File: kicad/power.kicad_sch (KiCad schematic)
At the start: 52 parts, among them P1 VBAT, P2 GND, P3 10V, P4 GND, Q2 NX7002AK, U1 LMR38020FSDDAR, U2 LMR38020FSDDAR, U4 LP38692MP-3.3, U5 LP5907MFX-3.3

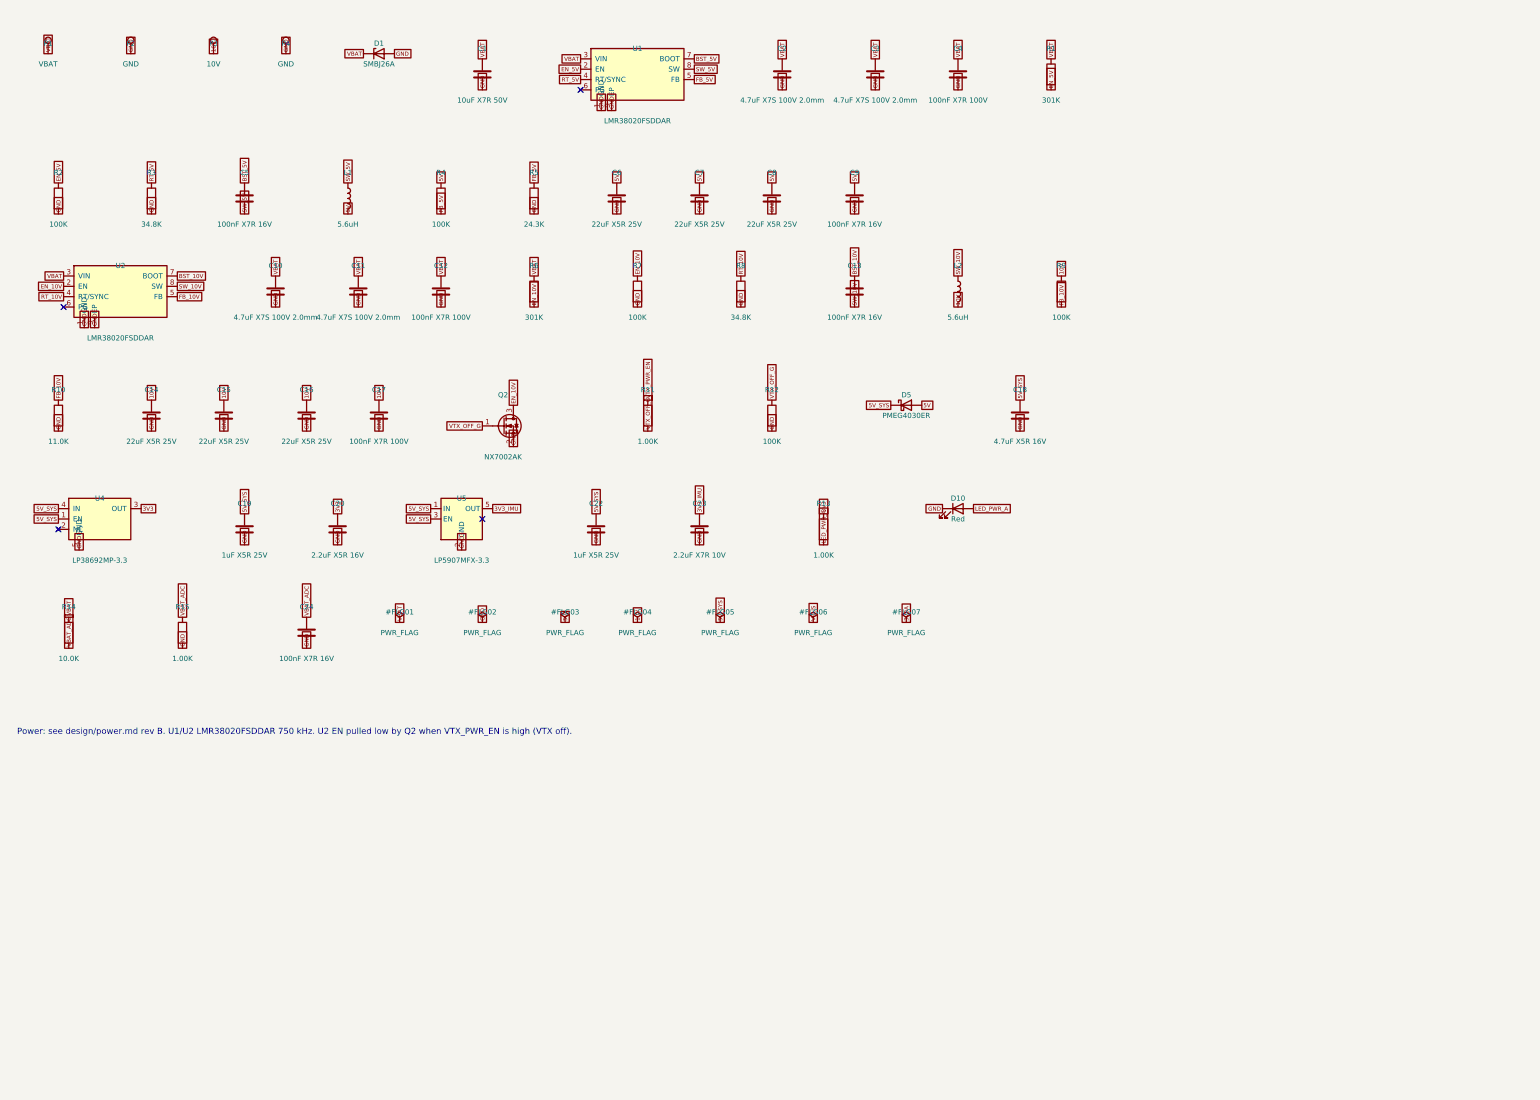
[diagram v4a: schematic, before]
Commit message: Readable schematic: functional blocks with titles, passives wired to their IC pins, GND power symbols, per-rail decoupling banks, labels only between blocks (ERC 0, netcheck OK, same nets)
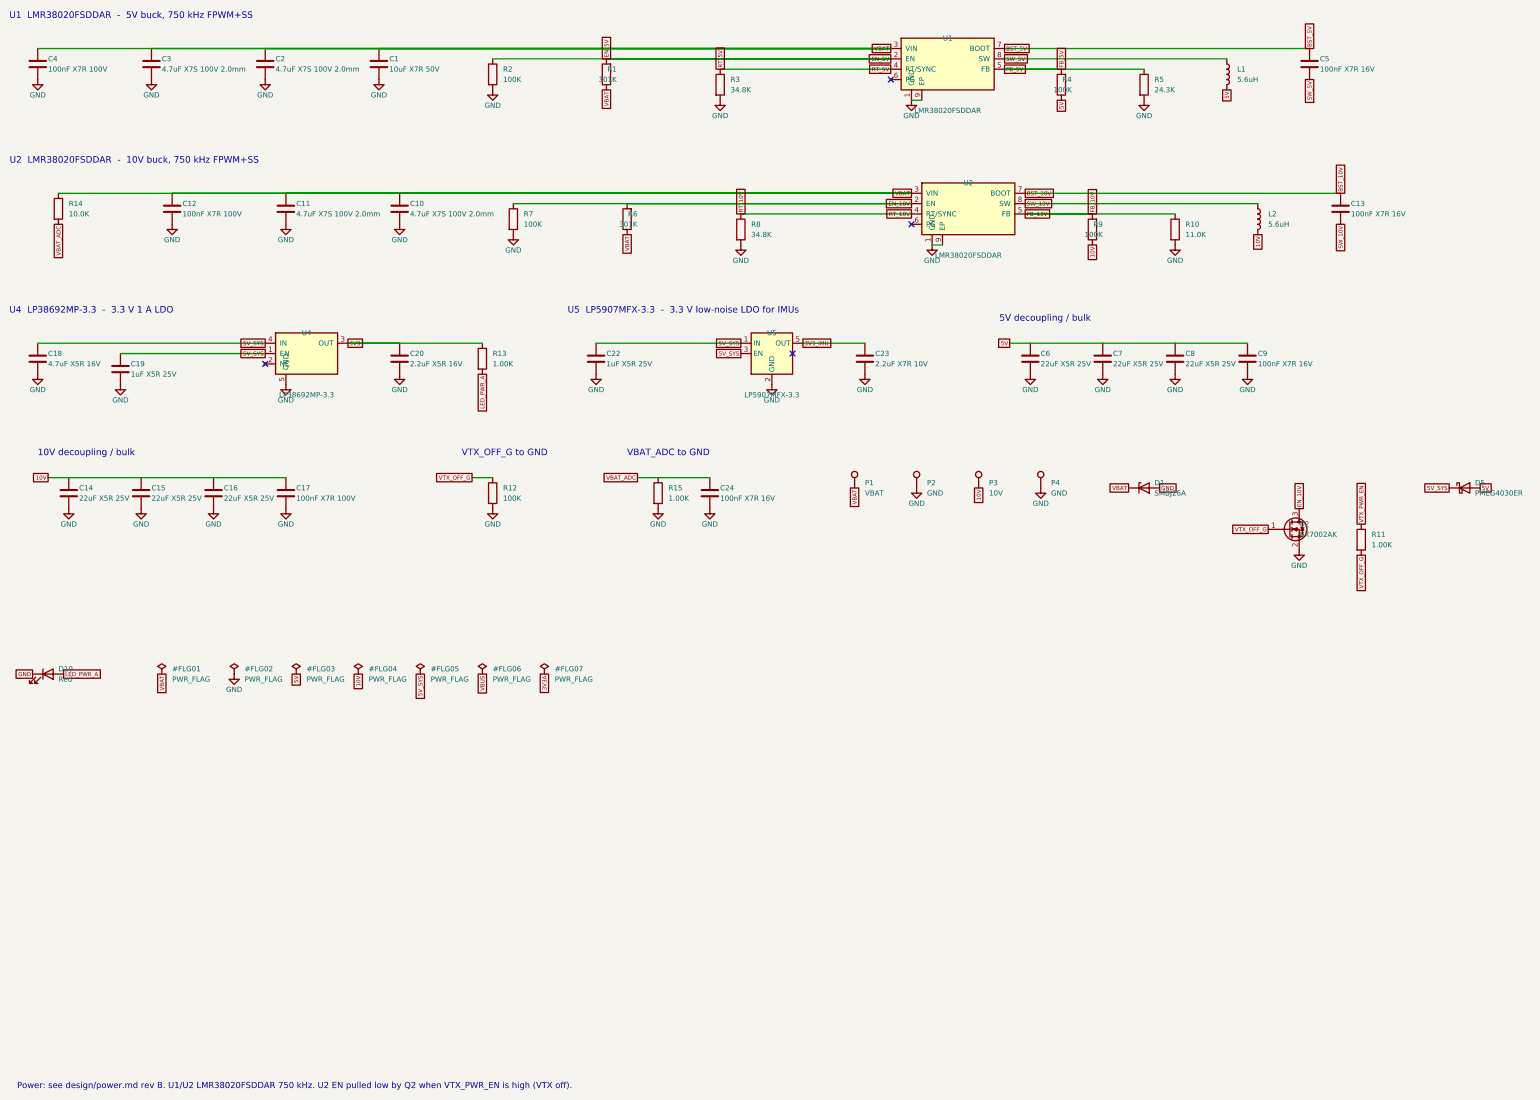
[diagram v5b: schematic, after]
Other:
- note added: "10V decoupling / bulk"
- note added: "5V decoupling / bulk"
- note added: "U1 LMR38020FSDDAR - 5V buck, 750 kHz FPWM+SS"
- note added: "U2 LMR38020FSDDAR - 10V buck, 750 kHz FPWM+SS"
- note added: "U4 LP38692MP-3.3 - 3.3 V 1 A LDO"
- note added: "U5 LP5907MFX-3.3 - 3.3 V low-noise LDO for IMUs"
- note added: "VBAT_ADC to GND"
- note added: "VTX_OFF_G to GND"
- moved on the sheet: C1, C10, C11, C12, C13, C14, C15, C16, C17, C18, C19, C2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

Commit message: Schematic regenerated for the L1/L2 WE-MAIA MPN (ERC 0, netcheck OK)
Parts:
- L1, L2: DigiKey not confirmed; alt 78438356056 = 732-11317-1-ND -> 732-11317-1-ND; MPN 74438356056 -> 78438356056
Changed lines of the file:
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@@
 			)
 		)
-		(property "Datasheet" "https://www.we-online.com/components/products/datasheet/74438356056.pdf"
+		(property "Datasheet" "https://www.we-online.com/components/products/datasheet/78438356056.pdf"
 			(at 312.42 35.56 0)
 			(effects
@@
 			)
 		)
-		(property "MPN" "74438356056"
+		(property "MPN" "78438356056"
 			(at 312.42 35.56 0)
 			(effects
@@
 			)
 		)
-		(property "DigiKey" "not confirmed; alt 78438356056 = 732-11317-1-ND"
+		(property "DigiKey" "732-11317-1-ND"
 			(at 312.42 35.56 0)
 			(effects
@@
 			)
 		)
-		(property "Datasheet" "https://www.we-online.com/components/products/datasheet/74438356056.pdf"
+		(property "Datasheet" "https://www.we-online.com/components/products/datasheet/78438356056.pdf"
 			(at 320.04 71.12 0)
 			(effects
@@
 			)
 		)
-		(property "MPN" "74438356056"
+		(property "MPN" "78438356056"
 			(at 320.04 71.12 0)
 			(effects
@@
 			)
 		)
-		(property "DigiKey" "not confirmed; alt 78438356056 = 732-11317-1-ND"
+		(property "DigiKey" "732-11317-1-ND"
 			(at 320.04 71.12 0)
 			(effects
